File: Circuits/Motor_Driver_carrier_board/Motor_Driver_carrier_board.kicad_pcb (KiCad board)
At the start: 2 copper layers, 35 x 55.6 mm, 21 parts, among them P2 61301021021

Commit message: Step file for mainboard pcb updated layout
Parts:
- moved P2 0.28 mm to (151.2, 69.7)
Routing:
- net /OUT2: track 38.9 -> 40.2 mm
- net /H3: track 18.3 -> 18.8 mm
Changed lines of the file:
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@@
 	(footprint "61301021021:ESC_Adapter_pins_right_angle"
 		(layer "F.Cu")
-		(at 150.92 69.65 90)
+		(at 151.2 69.65 90)
 		(descr "Pin Header, pitch 2.54 mm, THT, Angled, dual row, 10p")
 		(property "Reference" "P2"
@@
 		)
 	)
-	(gr_rect
-		(start 118.85 41.34)
-		(end 153.89 97.2)
-		(stroke
-			(width 0.5)
-			(type default)
-		)
-		(fill none)
-		(layer "Eco1.User")
-	)
 	(gr_line
 		(start 148.92 97.07)
@@
 	)
 	(segment
-		(start 134.3 46.7)
-		(end 133.3 46.7)
+		(start 151.82083 54.475896)
+		(end 151.82083 51.711308)
+		(width 1.79166)
+		(layer "B.Cu")
+		(net 3)
+	)
+	(segment
+		(start 151.82083 51.711308)
+		(end 144.717862 44.60834)
 		(width 1.79166)
 		(layer "B.Cu")
@@
 	(segment
 		(start 134.3 46.7)
-		(end 136.39166 44.60834)
+		(end 133.3 46.7)
 		(width 1.79166)
 		(layer "B.Cu")
@@
 	)
 	(segment
-		(start 133.8 44.6)
-		(end 133.8 46.2)
+		(start 144.717862 44.60834)
+		(end 136.39166 44.60834)
 		(width 1.79166)
 		(layer "B.Cu")
@@
 	)
 	(segment
-		(start 151.54083 51.711308)
-		(end 151.54083 53.95917)
+		(start 134.3 46.7)
+		(end 136.39166 44.60834)
 		(width 1.79166)
 		(layer "B.Cu")
@@
 	)
 	(segment
-		(start 151.54083 53.95917)
-		(end 150.17 55.33)
+		(start 133.8 44.6)
+		(end 133.8 46.2)
 		(width 1.79166)
 		(layer "B.Cu")
@@
 	)
 	(segment
-		(start 144.437862 44.60834)
-		(end 151.54083 51.711308)
+		(start 150.966726 55.33)
+		(end 151.82083 54.475896)
 		(width 1.79166)
 		(layer "B.Cu")
@@
 	)
 	(segment
-		(start 136.39166 44.60834)
-		(end 144.437862 44.60834)
+		(start 149.8 55.33)
+		(end 150.966726 55.33)
 		(width 1.79166)
 		(layer "B.Cu")
@@
 	)
 	(segment
-		(start 150.8 79.7)
-		(end 150.05 79.7)
+		(start 151.3 74.2)
+		(end 151.3 78.45)
 		(width 0.2)
 		(layer "F.Cu")
@@
 	)
 	(segment
-		(start 148.3 71.2)
-		(end 150.8 73.7)
-		(width 0.2)
-		(layer "F.Cu")
-		(net 9)
-	)
-	(segment
-		(start 150.05 79.7)
+		(start 151.3 78.45)
 		(end 149.52 80.23)
 		(width 0.2)
@@
 	)
 	(segment
-		(start 150.8 73.7)
-		(end 150.8 79.7)
+		(start 148.3 71.2)
+		(end 151.3 74.2)
 		(width 0.2)
 		(layer "F.Cu")
@@
 	)
 	(segment
-		(start 146.8 70.7)
-		(end 147.3 70.2)
+		(start 148.7 70.6)
+		(end 151.8 73.7)
 		(width 0.2)
 		(layer "F.Cu")
@@
 	)
 	(segment
-		(start 148.148529 70.2)
-		(end 151.3 73.351471)
+		(start 148.051471 70.6)
+		(end 148.7 70.6)
 		(width 0.2)
 		(layer "F.Cu")
@@
 	)
 	(segment
-		(start 151.3 73.351471)
-		(end 151.3 80.99)
+		(start 151.8 73.7)
+		(end 151.8 80.49)
 		(width 0.2)
 		(layer "F.Cu")
@@
 	)
 	(segment
-		(start 147.3 70.2)
-		(end 148.148529 70.2)
+		(start 151.8 80.49)
+		(end 149.52 82.77)
 		(width 0.2)
 		(layer "F.Cu")
@@
 	)
 	(segment
-		(start 151.3 80.99)
-		(end 149.52 82.77)
+		(start 146.8 71.2)
+		(end 147.3 70.7)
+		(width 0.2)
+		(layer "F.Cu")
+		(net 12)
+	)
+	(segment
+		(start 147.951471 70.7)
+		(end 148.051471 70.6)
+		(width 0.2)
+		(layer "F.Cu")
+		(net 12)
+	)
+	(segment
+		(start 147.3 70.7)
+		(end 147.951471 70.7)
 		(width 0.2)
 		(layer "F.Cu")
@@
 	)
 	(via
-		(at 146.8 70.7)
+		(at 146.8 71.2)
 		(size 0.6)
 		(drill 0.3)
@@
 	)
 	(segment
-		(start 146.6 70.5)
-		(end 146.8 70.7)
+		(start 146.8 71.2)
+		(end 146.1 70.5)
 		(width 0.2)
 		(layer "B.Cu")
@@
 	)
 	(segment
-		(start 144.8 70.5)
-		(end 146.6 70.5)
+		(start 146.1 70.5)
+		(end 144.8 70.5)
 		(width 0.2)
 		(layer "B.Cu")

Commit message: STP to pointer
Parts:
- P2: value 61301021021 -> ESC_Adapter_pins_right_angle; footprint 61301021021:ESC_Adapter_pins_right_angle -> B-G431B-ESC1:ESC_Adapter_pins_right_angle
- moved P2 5.95 mm to (154.8, 74.4)
- moved +3.3V 1.11 mm to (122.9, 85.1)
- moved GND 1.11 mm to (122.9, 87.0)
- moved SWCLK 1.11 mm to (122.9, 83.2)
- moved SWDIO 1.11 mm to (122.9, 81.3)
- moved J3 1.00 mm to (121.8, 67.2)
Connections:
- net /3.3V renamed 3.3V
- net /SWCLK renamed SWCLK
- net /SWDIO renamed SWDIO
- +24V pad 1: /24V -> 24V
- 5V pad 1: /5V -> 5V (x2)
- GND pad 1: GND -> UART_GND
- H1 pad 1: /H1 -> H1
- H2 pad 1: /H2 -> H2
- H3 pad 1: /H3 -> H3
- OUT1 pad 1: /OUT1 -> OUT1
- OUT2 pad 1: /OUT2 -> OUT2
- OUT3 pad 1: /OUT3 -> OUT3
- P2 pad 1: /OUT1 -> OUT1
- P2 pad 10: GND -> OUT3
- P2 pad 11: /H1 -> OUT3
- P2 pad 12: /PWM -> OUT3
- P2 pad 13: /H2 -> 24V
- P2 pad 14: /RX -> 24V
- P2 pad 15: /H3 -> 24V
- P2 pad 16: /TX -> 24V
- P2 pad 17: /5V -> GND
- P2 pad 18: /5V -> GND
- P2 pad 2: /OUT1 -> OUT1
- P2 pad 3: /OUT2 -> OUT1
- P2 pad 4: /OUT2 -> OUT1
- P2 pad 5: /OUT3 -> OUT2
- P2 pad 6: /OUT3 -> OUT2
- P2 pad 7: /24V -> OUT2
- P2 pad 8: /24V -> OUT2
- P2 pad 9: GND -> OUT3
- PWM pad 1: /PWM -> PWM
- RX pad 1: /RX -> RX
- TX pad 1: /TX -> TX
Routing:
- net 5V: track 0.00 -> 73.4 mm, vias 0 -> 1
- net OUT1: track 0.00 -> 60.5 mm
- net OUT3: track 0.00 -> 43.6 mm
- net /5V: track 43.2 -> 0.00 mm, vias 2 -> 0
- net OUT2: track 0.00 -> 42.9 mm
- net /OUT2: track 40.2 -> 0.00 mm, vias 10 -> 0
- net /24V: track 37.7 -> 0.00 mm
- net /OUT1: track 30.0 -> 0.00 mm
- net RX: track 0.00 -> 29.9 mm
- net TX: track 0.00 -> 28.5 mm
- net /TX: track 26.0 -> 0.00 mm, vias 2 -> 0
- net /PWM: track 25.9 -> 0.00 mm, vias 2 -> 0
- net /RX: track 25.9 -> 0.00 mm, vias 2 -> 0
- net H1: track 0.00 -> 23.1 mm
- net /OUT3: track 22.1 -> 0.00 mm, vias 10 -> 0
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- added copper zone on F.Cu, net 24V
- removed copper zone on F.Cu, net GND
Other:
- board size 35 x 55.6 mm -> 40.2 x 62.7 mm

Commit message: Exported mainboard, carrier board, and encoder to gerber
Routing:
- net 24V: track 1.06 -> 24.0 mm
- net GND: track 14.7 -> 24.6 mm, vias 2 -> 7
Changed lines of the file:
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@@
+	)
+	(via
+		(at 124.11 91.92)
+		(size 1.2)
+		(drill 1)
+		(layers "F.Cu" "B.Cu")
+		(net 1)
+	)
+	(via
+		(at 125.79 91.91)
+		(size 1.2)
+		(drill 1)
+		(layers "F.Cu" "B.Cu")
+		(net 1)
+	)
+	(via
+		(at 127.44 91.95)
+		(size 1.2)
+		(drill 1)
+		(layers "F.Cu" "B.Cu")
+		(net 1)
 	)
 	(via
@@
 	)
 	(via
+		(at 127.44 93.37)
+		(size 1.2)
+		(drill 1)
+		(layers "F.Cu" "B.Cu")
+		(net 1)
+	)
+	(via
+		(at 124.11 93.36)
+		(size 1.2)
+		(drill 1)
+		(layers "F.Cu" "B.Cu")
+		(net 1)
+	)
+	(via
 		(at 125.8 93.3)
 		(size 1.2)
@@
 	)
 	(segment
-		(start 150.66 66.67)
-		(end 150.66 69.21)
+		(start 155.25 68.545)
+		(end 153.375 66.67)
 		(width 2)
 		(layer "B.Cu")
@@
 	)
 	(segment
+		(start 149.99 67.88)
+		(end 151.45 69.34)
+		(width 2)
+		(layer "B.Cu")
+		(net 1)
+	)
+	(segment
 		(start 153.2 66.67)
 		(end 150.66 66.67)
@@
 	)
 	(segment
+		(start 150.66 67.88)
+		(end 150.66 69.21)
+		(width 2)
+		(layer "B.Cu")
+		(net 1)
+	)
+	(segment
 		(start 153.2 66.67)
 		(end 153.2 69.21)
@@
 	)
 	(segment
+		(start 151.45 69.34)
+		(end 155.25 69.34)
+		(width 2)
+		(layer "B.Cu")
+		(net 1)
+	)
+	(segment
+		(start 150.66 67.88)
+		(end 149.99 67.88)
+		(width 2)
+		(layer "B.Cu")
+		(net 1)
+	)
+	(segment
+		(start 155.25 69.34)
+		(end 155.25 68.545)
+		(width 2)
+		(layer "B.Cu")
+		(net 1)
+	)
+	(segment
 		(start 150.66 69.21)
 		(end 153.2 66.67)
+		(width 2)
+		(layer "B.Cu")
+		(net 1)
+	)
+	(segment
+		(start 150.66 66.67)
+		(end 150.66 67.88)
 		(width 2)
 		(layer "B.Cu")
@@
 	)
 	(segment
-		(start 154.9 76.8)
-		(end 154.9 83.465)
+		(start 153.14 80.31166)
+		(end 154.55 81.72166)
 		(width 0.3)
 		(layer "B.Cu")
@@
 	)
 	(segment
+		(start 153.14 75.04)
+		(end 153.14 80.31166)
+		(width 0.3)
+		(layer "B.Cu")
+		(net 9)
+	)
+	(segment
+		(start 154.55 83.815)
+		(end 153.375 84.99)
+		(width 0.3)
+		(layer "B.Cu")
+		(net 9)
+	)
+	(segment
+		(start 154.55 81.72166)
+		(end 154.55 83.815)
+		(width 0.3)
+		(layer "B.Cu")
+		(net 9)
+	)
+	(segment
 		(start 144.8 66.7)
-		(end 154.9 76.8)
-		(width 0.3)
-		(layer "B.Cu")
-		(net 9)
-	)
-	(segment
-		(start 154.9 83.465)
-		(end 153.375 84.99)
+		(end 153.14 75.04)
 		(width 0.3)
 		(layer "B.Cu")
@@
 	)
 	(segment
+		(start 155.14 61.59)
+		(end 155.18 61.55)
+		(width 2)
+		(layer "F.Cu")
+		(net 12)
+	)
+	(segment
+		(start 153.375 64.13)
+		(end 150.835 64.13)
+		(width 2)
+		(layer "F.Cu")
+		(net 12)
+	)
+	(segment
+		(start 155.18 62.325)
+		(end 153.375 64.13)
+		(width 2)
+		(layer "F.Cu")
+		(net 12)
+	)
+	(segment
+		(start 153.375 64.13)
+		(end 150.835 61.59)
+		(width 2)
+		(layer "F.Cu")
+		(net 12)
+	)
+	(segment
+		(start 148.67 61.965)
+		(end 150.835 64.13)
+		(width 2)
+		(layer "F.Cu")
+		(net 12)
+	)
+	(segment
+		(start 150.835 64.13)
+		(end 153.375 61.59)
+		(width 2)
+		(layer "F.Cu")
+		(net 12)
+	)
+	(segment
+		(start 153.375 61.59)
+		(end 155.14 61.59)
+		(width 2)
+		(layer "F.Cu")
+		(net 12)
+	)
+	(segment
+		(start 150.835 61.59)
+		(end 148.83 61.59)
+		(width 2)
+		(layer "F.Cu")
+		(net 12)
+	)
+	(segment
+		(start 148.83 61.59)
+		(end 148.67 61.75)
+		(width 2)
+		(layer "F.Cu")
+		(net 12)
+	)
+	(segment
 		(start 142.3 92.7)
 		(end 143.357362 92.7)
+		(width 2)
+		(layer "F.Cu")
+		(net 12)
+	)
+	(segment
+		(start 148.67 61.75)
+		(end 148.67 61.965)
+		(width 2)
+		(layer "F.Cu")
+		(net 12)
+	)
+	(segment
+		(start 155.18 61.55)
+		(end 155.18 62.325)
+		(width 2)
+		(layer "F.Cu")
+		(net 12)
+	)
+	(segment
+		(start 150.835 61.59)
+		(end 153.375 61.59)
 		(width 2)
 		(layer "F.Cu")
@@
 	)
 	(segment
+		(start 145.45 68.6)
+		(end 152.52 75.67)
+		(width 0.3)
+		(layer "B.Cu")
+		(net 16)
+	)
+	(segment
 		(start 144.8 68.6)
 		(end 145.45 68.6)
@@
 	)
 	(segment
-		(start 145.45 68.6)
-		(end 153.375 76.525)
+		(start 152.52 75.67)
+		(end 152.52 81.595)
 		(width 0.3)
 		(layer "B.Cu")
@@
 	)
 	(segment
-		(start 153.375 76.525)
+		(start 152.52 81.595)
 		(end 153.375 82.45)
 		(width 0.3)

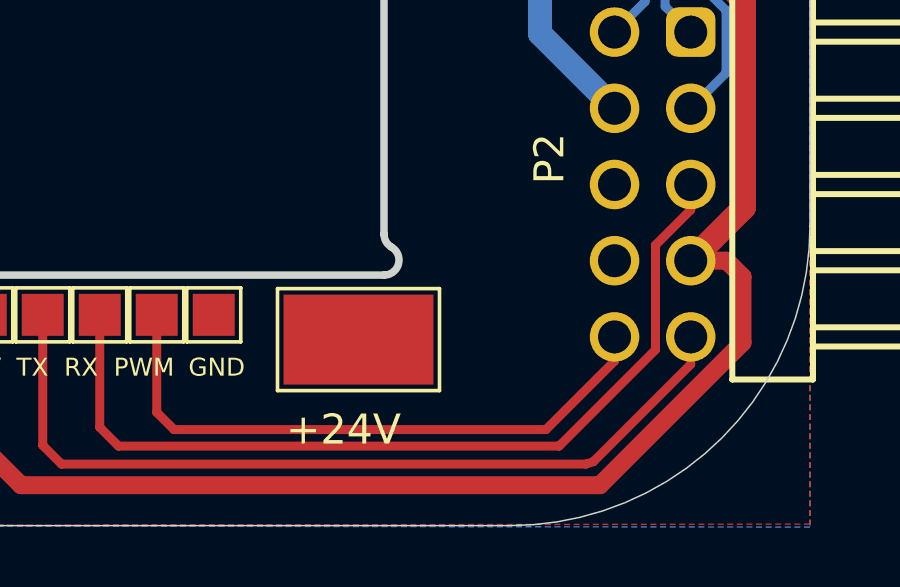
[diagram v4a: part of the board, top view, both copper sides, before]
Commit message: Added 3 models to the pcbs
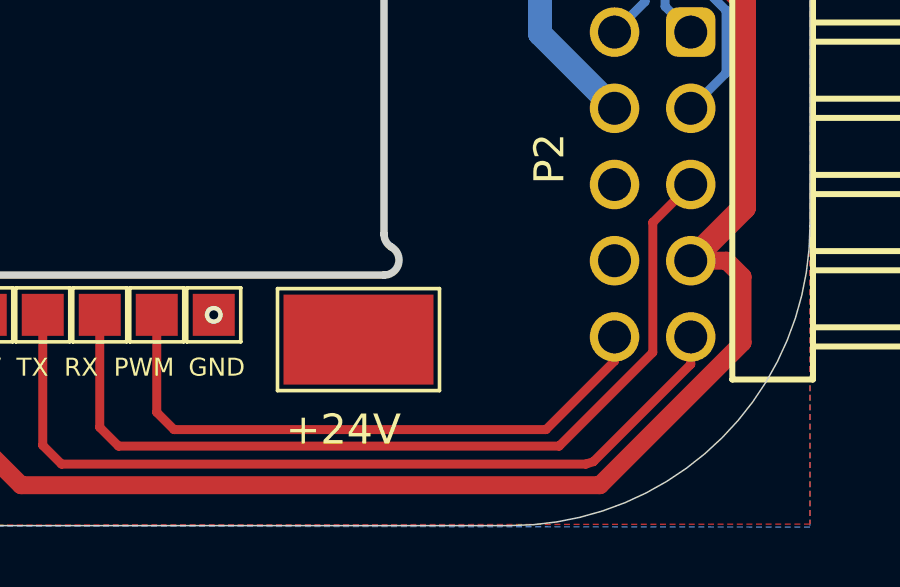
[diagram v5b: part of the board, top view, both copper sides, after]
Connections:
- GND pad 1: UART_GND -> GND
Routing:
- net GND: track 24.6 -> 25.0 mm, vias 7 -> 8
